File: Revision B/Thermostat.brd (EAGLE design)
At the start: 50.8 x 50.8 mm, 27 parts

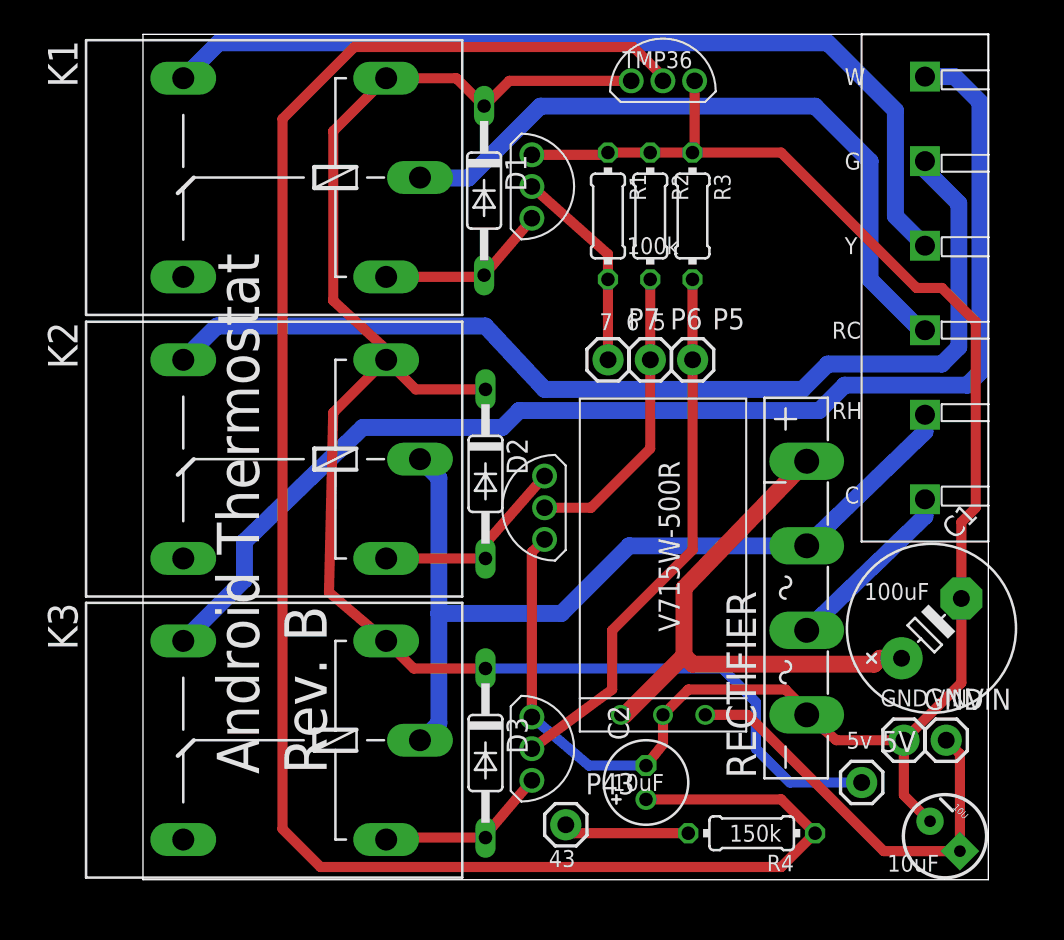
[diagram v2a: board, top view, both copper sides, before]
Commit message: Low-pass filter changes
Made adjustments to the low-pass filter per suggestions at:
http://www.reddit.com/r/AndroidThermostat/comments/19ntz4/temp_sensor_filter/
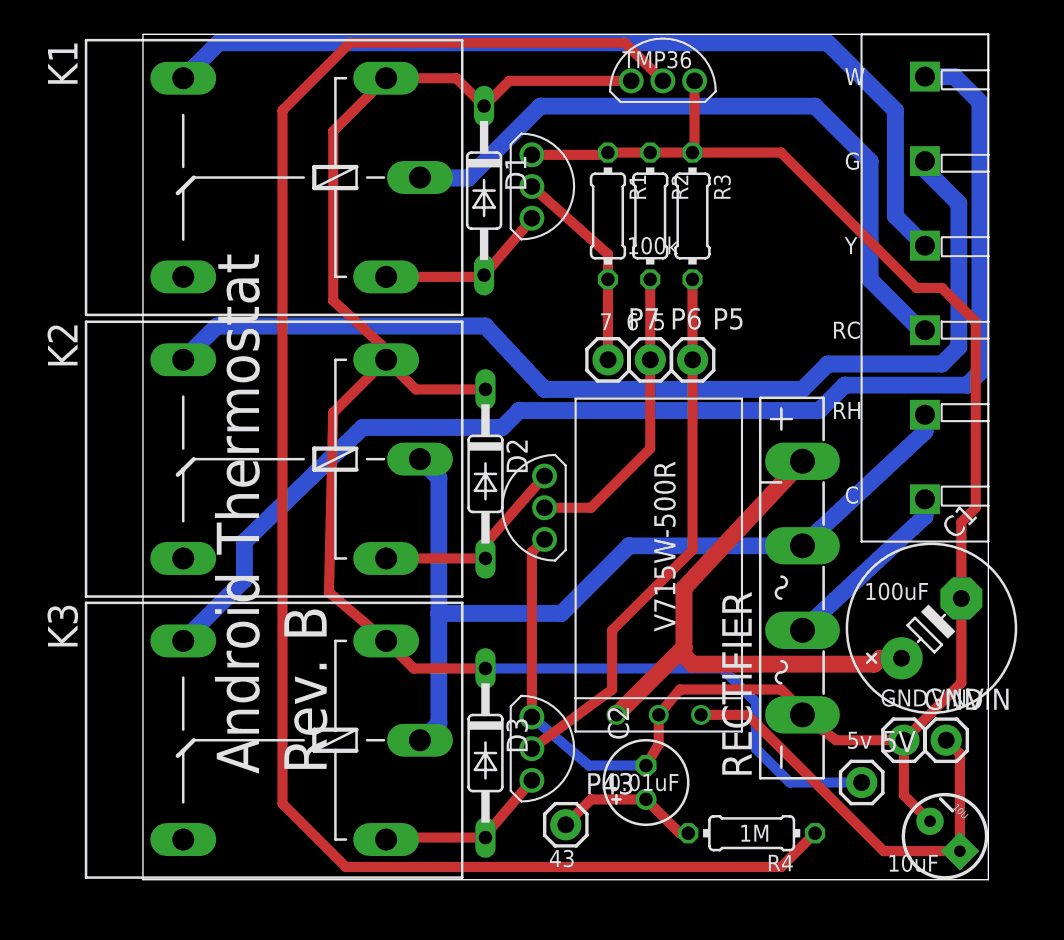
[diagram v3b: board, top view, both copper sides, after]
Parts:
- moved RECTIFIER 0.25 mm to (39.6, 17.5)
- moved U$2 0.25 mm to (31.0, 9.91)
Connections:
- net N$4: now also P43.1, R4.2; no longer R4.1, U$1.OUT2
- net N$5: now also R4.1, U$1.OUT2; no longer P43.1, R4.2
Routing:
- net N$4: track 113.1 -> 8.83 mm
- net N$5: track 7.57 -> 101.6 mm
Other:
- board text added: "0.01uF"
- board text added: "1M"
- board text removed: "150k"
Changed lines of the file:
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@@
 <text x="8.4963" y="6.35" size="2.54" layer="122" font="vector" rot="MR90">Android Thermostat</text>
 <text x="4.572" y="6.096" size="2.54" layer="122" font="vector" rot="MR90">Rev. B</text>
-<text x="28.194" y="5.334" size="1.016" layer="121" font="vector">10uF</text>
-<text x="38.354" y="3.302" size="1.016" layer="121" font="vector" rot="R180">150k</text>
 <text x="27.432" y="33.02" size="1.016" layer="121" font="vector">7  6  5</text>
 <text x="24.384" y="0.762" size="1.016" layer="121" font="vector">43</text>
@@
 <text x="41.402" y="27.686" size="1.016" layer="121" font="vector">RH</text>
 <text x="42.164" y="22.606" size="1.016" layer="121" font="vector">C</text>
+<text x="27.94" y="5.334" size="1.016" layer="121" font="vector">0.01uF</text>
+<text x="35.814" y="2.286" size="1.016" layer="121" font="vector">1M</text>
 </plain>
 <attributes>
@@
 </autorouter>
 <elements>
-<element name="RECTIFIER" library="rectifier" package="GBU4S" value="" x="39.8843" y="17.526" rot="R90"/>
+<element name="RECTIFIER" library="rectifier" package="GBU4S" value="" x="39.6303" y="17.526" rot="R90"/>
 <element name="10U" library="SparkFun-Passives" package="CPOL-RADIAL-10UF-25V" value="" x="48.191903125" y="2.61439375" rot="R315"/>
 <element name="5V" library="SparkFun-Connectors" package="1X01" value="" x="43.1863" y="5.842"/>
@@
 <element name="P7" library="SparkFun-Connectors" package="1X01" value="" x="27.9463" y="31.242"/>
 <element name="VIN" library="SparkFun-Connectors" package="1X01" value="" x="48.2663" y="8.382"/>
-<element name="U$2" library="android-thermostat" package="SWITCHINGREGULATOR" value="V715W-500R" x="31.2483" y="9.906" rot="R90"/>
+<element name="U$2" library="android-thermostat" package="SWITCHINGREGULATOR" value="V715W-500R" x="30.9943" y="9.906" rot="R90"/>
 <element name="K1" library="relay" package="G5LE" value="" x="7.1183" y="42.19448125" rot="R180">
 <attribute name="OC_NEWARK" value="unknown" x="7.1183" y="42.19448125" size="1.778" layer="27" rot="R180" display="off"/>
@@
 <contactref element="U$3" pad="P$1"/>
 <wire x1="46.99" y1="22.86" x2="46.99" y2="21.8377" width="1.016" layer="16"/>
-<wire x1="46.99" y1="21.8377" x2="39.8843" y2="14.986" width="1.016" layer="16"/>
+<wire x1="46.99" y1="21.8377" x2="39.6303" y2="14.986" width="1.016" layer="16"/>
 </signal>
 <signal name="N$1">
@@
 <wire x1="49.176078125" y1="11.831778125" x2="45.7263" y2="8.382" width="0.6096" layer="1"/>
 <wire x1="45.7263" y1="8.382" x2="41.6623" y2="8.382" width="0.6096" layer="1"/>
-<wire x1="41.6623" y1="8.382" x2="39.8843" y2="9.906" width="0.6096" layer="1"/>
+<wire x1="41.6623" y1="8.382" x2="39.6303" y2="9.906" width="0.6096" layer="1"/>
 <wire x1="33.02" y1="43.6943" x2="30.48" y2="43.6943" width="0.6096" layer="1"/>
 <wire x1="30.48" y1="43.6943" x2="27.94" y2="43.6943" width="0.6096" layer="1"/>
@@
 <wire x1="23.368" y1="9.779" x2="23.368" y2="19.685" width="0.6096" layer="1"/>
 <wire x1="23.368" y1="19.685" x2="24.13" y2="20.447" width="0.6096" layer="1"/>
-<wire x1="39.8843" y1="9.906" x2="40.132" y2="9.906" width="0.6096" layer="1"/>
-<wire x1="40.132" y1="9.906" x2="38.608" y2="11.43" width="0.6096" layer="1"/>
-<wire x1="38.608" y1="11.43" x2="32.7723" y2="11.43" width="0.6096" layer="1"/>
-<wire x1="32.7723" y1="11.43" x2="31.2483" y2="9.906" width="0.6096" layer="1"/>
-<wire x1="31.2483" y1="9.906" x2="31.2483" y2="8.1343" width="0.6096" layer="1"/>
-<wire x1="31.2483" y1="8.1343" x2="30.226" y2="6.858" width="0.6096" layer="1"/>
+<wire x1="39.6303" y1="9.906" x2="39.878" y2="9.906" width="0.6096" layer="1"/>
+<wire x1="39.878" y1="9.906" x2="38.354" y2="11.43" width="0.6096" layer="1"/>
+<wire x1="38.354" y1="11.43" x2="32.2643" y2="11.43" width="0.6096" layer="1"/>
+<wire x1="32.2643" y1="11.43" x2="30.9943" y2="9.906" width="0.6096" layer="1"/>
+<wire x1="30.9943" y1="9.906" x2="30.9943" y2="8.1343" width="0.6096" layer="1"/>
+<wire x1="30.9943" y1="8.1343" x2="30.226" y2="6.858" width="0.6096" layer="1"/>
 <wire x1="33.147" y1="48.006" x2="33.147" y2="43.8213" width="0.6096" layer="1"/>
 <wire x1="33.147" y1="43.8213" x2="33.02" y2="43.6943" width="0.6096" layer="1"/>
@@
 <wire x1="49.089928125" y1="1.716365625" x2="44.511634375" y2="1.716365625" width="0.6096" layer="1"/>
 <wire x1="44.511634375" y1="1.716365625" x2="36.322" y2="9.906" width="0.6096" layer="1"/>
-<wire x1="36.322" y1="9.906" x2="33.7883" y2="9.906" width="0.6096" layer="1"/>
+<wire x1="36.322" y1="9.906" x2="33.5343" y2="9.906" width="0.6096" layer="1"/>
 </signal>
 <signal name="N$24">
@@
 <contactref element="RECTIFIER" pad="+"/>
 <contactref element="C1" pad="+"/>
-<wire x1="28.7083" y1="9.906" x2="28.9623" y2="9.9123" width="1.016" layer="1"/>
-<wire x1="28.9623" y1="9.9123" x2="32.512" y2="13.462" width="1.016" layer="1"/>
-<wire x1="32.512" y1="13.462" x2="32.512" y2="17.5197" width="1.016" layer="1"/>
-<wire x1="32.512" y1="17.5197" x2="39.8843" y2="25.146" width="1.016" layer="1"/>
+<wire x1="32.512" y1="13.462" x2="32.512" y2="13.97" width="1.016" layer="1"/>
+<wire x1="32.512" y1="13.97" x2="32.512" y2="17.5197" width="1.016" layer="1"/>
+<wire x1="32.512" y1="17.5197" x2="39.6303" y2="25.146" width="1.016" layer="1"/>
 <wire x1="45.583975" y1="13.307921875" x2="44.295921875" y2="13.307921875" width="1.016" layer="1"/>
 <wire x1="44.295921875" y1="13.307921875" x2="43.942" y2="12.954" width="1.016" layer="1"/>
 <wire x1="43.942" y1="12.954" x2="33.02" y2="12.954" width="1.016" layer="1"/>
 <wire x1="33.02" y1="12.954" x2="32.512" y2="13.462" width="1.016" layer="1"/>
-</signal>
-<signal name="N$4">
-<contactref element="C2" pad="+"/>
-<contactref element="U$1" pad="OUT2"/>
-<contactref element="R4" pad="1"/>
-<wire x1="30.226" y1="4.826" x2="38.354" y2="4.826" width="0.6096" layer="1"/>
-<wire x1="38.354" y1="4.826" x2="40.386" y2="2.794" width="0.6096" layer="1"/>
-<wire x1="31.242" y1="48.006" x2="31.242" y2="48.26" width="0.6096" layer="1"/>
-<wire x1="31.242" y1="48.26" x2="29.464" y2="50.038" width="0.6096" layer="1"/>
-<wire x1="29.464" y1="50.038" x2="12.7" y2="50.038" width="0.6096" layer="1"/>
-<wire x1="12.7" y1="50.038" x2="8.382" y2="45.72" width="0.6096" layer="1"/>
-<wire x1="8.382" y1="45.72" x2="8.382" y2="3.048" width="0.6096" layer="1"/>
-<wire x1="8.382" y1="3.048" x2="10.668" y2="0.762" width="0.6096" layer="1"/>
-<wire x1="10.668" y1="0.762" x2="38.354" y2="0.762" width="0.6096" layer="1"/>
-<wire x1="38.354" y1="0.762" x2="40.386" y2="2.794" width="0.6096" layer="1"/>
-</signal>
-<signal name="N$5">
-<contactref element="P43" pad="1"/>
-<contactref element="R4" pad="2"/>
-<wire x1="32.766" y1="2.794" x2="25.9143" y2="2.794" width="0.6096" layer="1"/>
-<wire x1="25.9143" y1="2.794" x2="25.4063" y2="3.302" width="0.6096" layer="1"/>
+<wire x1="28.4543" y1="9.906" x2="28.4543" y2="9.9123" width="1.016" layer="1"/>
+<wire x1="28.4543" y1="9.9123" x2="32.512" y2="13.97" width="1.016" layer="1"/>
 </signal>
 <signal name="N$9">
@@
 <contactref element="K2" pad="P"/>
 <wire x1="46.99" y1="27.94" x2="46.99" y2="26.9177" width="1.016" layer="16"/>
-<wire x1="46.99" y1="26.9177" x2="39.8843" y2="20.066" width="1.016" layer="16"/>
+<wire x1="46.99" y1="26.9177" x2="39.6303" y2="20.066" width="1.016" layer="16"/>
 <wire x1="16.6433" y1="8.382" x2="16.764" y2="8.382" width="1.016" layer="16"/>
 <wire x1="16.764" y1="8.382" x2="17.78" y2="9.398" width="1.016" layer="16"/>
@@
 <wire x1="17.78" y1="16.002" x2="17.78" y2="24.1363" width="1.016" layer="16"/>
 <wire x1="17.78" y1="24.1363" x2="16.6433" y2="25.273" width="1.016" layer="16"/>
-<wire x1="39.8843" y1="20.066" x2="29.21" y2="20.066" width="1.016" layer="16"/>
+<wire x1="39.6303" y1="20.066" x2="29.21" y2="20.066" width="1.016" layer="16"/>
 <wire x1="29.21" y1="20.066" x2="25.146" y2="16.002" width="1.016" layer="16"/>
 <wire x1="25.146" y1="16.002" x2="17.78" y2="16.002" width="1.016" layer="16"/>
 </signal>
+<signal name="N$4">
+<contactref element="R4" pad="2"/>
+<contactref element="C2" pad="+"/>
+<contactref element="P43" pad="1"/>
+<wire x1="32.766" y1="2.794" x2="32.258" y2="2.794" width="0.6096" layer="1"/>
+<wire x1="32.258" y1="2.794" x2="30.226" y2="4.826" width="0.6096" layer="1"/>
+<wire x1="30.226" y1="4.826" x2="26.9303" y2="4.826" width="0.6096" layer="1"/>
+<wire x1="26.9303" y1="4.826" x2="25.4063" y2="3.302" width="0.6096" layer="1"/>
+</signal>
+<signal name="N$5">
+<contactref element="U$1" pad="OUT2"/>
+<contactref element="R4" pad="1"/>
+<wire x1="31.242" y1="48.006" x2="28.956" y2="50.292" width="0.6096" layer="1"/>
+<wire x1="28.956" y1="50.292" x2="12.446" y2="50.292" width="0.6096" layer="1"/>
+<wire x1="12.446" y1="50.292" x2="8.382" y2="46.228" width="0.6096" layer="1"/>
+<wire x1="8.382" y1="46.228" x2="8.382" y2="4.572" width="0.6096" layer="1"/>
+<wire x1="8.382" y1="4.572" x2="12.192" y2="0.762" width="0.6096" layer="1"/>
+<wire x1="12.192" y1="0.762" x2="38.354" y2="0.762" width="0.6096" layer="1"/>
+<wire x1="38.354" y1="0.762" x2="40.386" y2="2.794" width="0.6096" layer="1"/>
+</signal>
 </signals>
